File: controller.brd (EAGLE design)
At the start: 100 x 80 mm, 14 parts, among them IC1 7805DT, J1 POWER_JACKSLT, Q1 MOSFET-NCHANNELBSS123LT1G, Q2 MOSFET-PCHANNELSMD

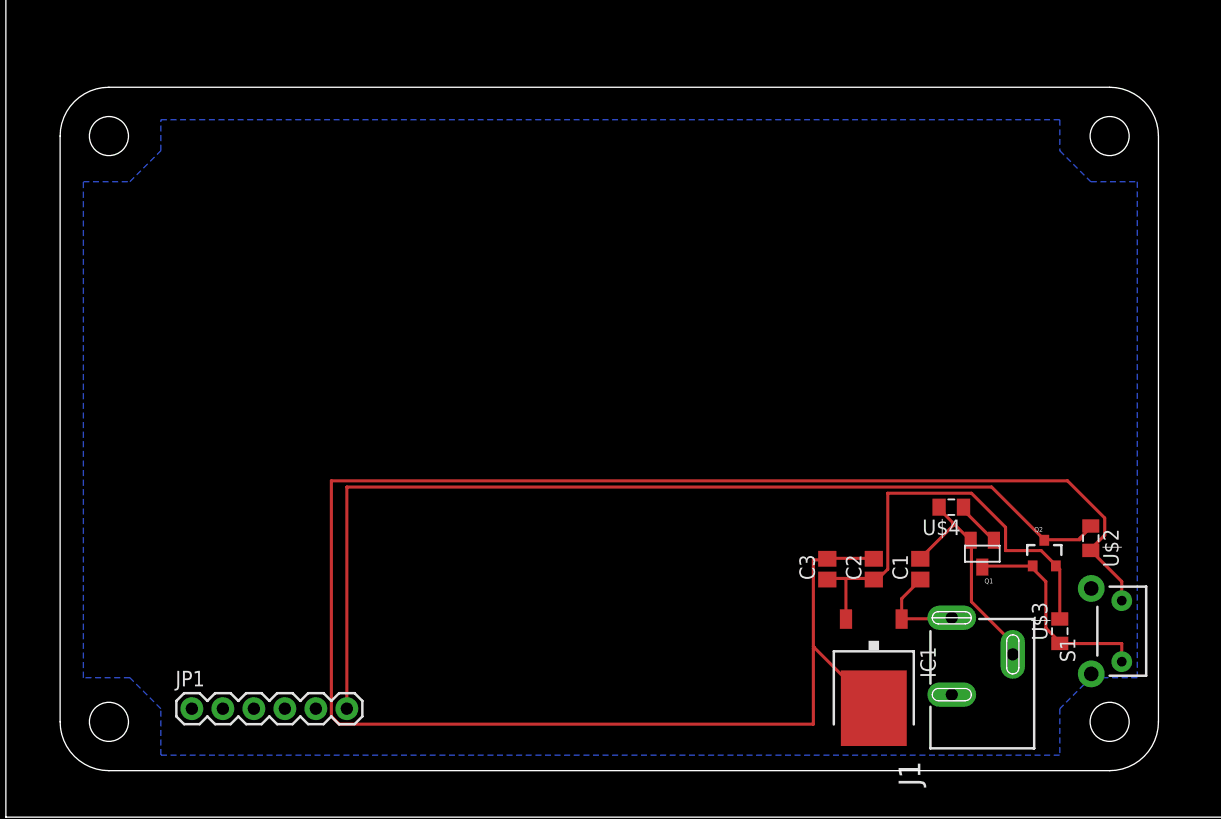
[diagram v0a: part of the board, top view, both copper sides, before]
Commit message: removed parts order from repo
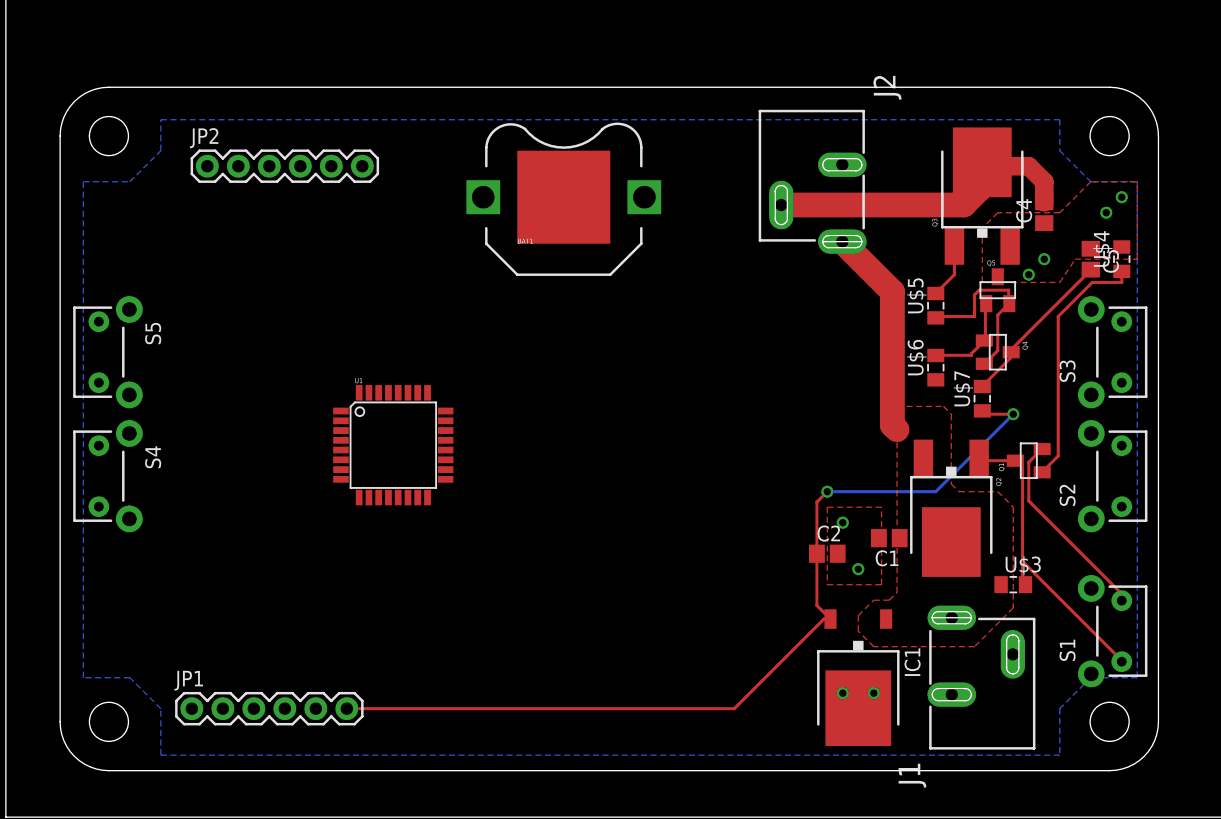
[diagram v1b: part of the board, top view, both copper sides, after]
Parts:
- removed C3: (no value), adafruit:C0805
- removed U$2: (no value), jt_parts:RESISTOR-0805
- added BAT1: (no value), SparkFun-Electromechanical:BATTCON_12MM_PTH
- added C4, C5: (no value), adafruit:C0805
- added J2: POWER_JACKSLT, SparkFun-Connectors:POWER_JACK_SLOT
- added JP2: (no value), SparkFun-Connectors:1X06
- added Q3: MOSFET-NCHANNELFDD8780, SparkFun-DiscreteSemi:DPAK
- added Q4: (no value), SparkFun-DiscreteSemi:SOT23
- added Q5: MMBT4403, SparkFun-DiscreteSemi:SOT23
- added S2, S3, S4, S5: SWITCH-MOMENTARY-2SIDE_EZ, SparkFun-Electromechanical:TACTILE-PTH-SIDEEZ
- added U$5, U$6, U$7: (no value), jt_parts:RESISTOR-0805
- added U1: ATMEGA328P, SparkFun-DigitalIC:TQFP32-08
- Q2: value MOSFET-PCHANNELSMD -> MOSFET-NCHANNELFDD8780; device SparkFun-DiscreteSemi:SOT23-3 -> SparkFun-DiscreteSemi:DPAK
- U$3, U$4: value (none) -> 10k
- moved U$4 24.7 mm to (91.4, 45.7), turned to 90 degrees
- moved Q1 8.52 mm to (83.8, 29.2), turned to 90 degrees
- moved Q2 8.03 mm to (77.5, 24.1), turned to 180 degrees
- moved U$3 5.39 mm to (82.5, 19.1), turned to 0 degrees
- moved C2 4.02 mm to (67.3, 21.6), turned to 0 degrees
- moved C1 3.59 mm to (72.4, 22.9), turned to 180 degrees
- moved IC1 1.27 mm to (69.8, 11.4)
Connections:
- net GATE-MCU renamed PWR-CNTRL
- removed net N$1: C2.1, C3.1, IC1.2, Q2.2, U$3.2
- new net +: BAT1.VCC@1
- new net -: BAT1.GND
- new net 12V-IN: J1.PWR, Q2.4, U$3.1
- new net N$10: Q1.3, Q2.1, S1.1, U$3.2
- new net N$3: Q3.1, U$5.2
- new net N$4: C4.2, J2.GND@2, Q3.4
- new net N$5: Q4.2, Q5.2, U$5.1
- new net NONE: Q4.1, Q5.1, U$6.2
- new net PWM: U$6.1
- net 12V: now also J2.PWR, Q2.3; no longer J1.PWR
- net 5V: now also C2.1, IC1.2, U$7.1; no longer Q2.3, U$2.1
- net GND: now also C4.1, C5.1, Q3.3, Q5.3; no longer C3.2, U$2.2
- net N$2: now also C5.2, Q4.3, U$7.2; no longer Q1.3, Q2.1, S1.1, U$3.1
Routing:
- net GND: track 176.3 -> 19.6 mm, vias 0 -> 8
- net N$1: track 36.9 -> 0.00 mm
- net N$4: track 0.00 -> 26.5 mm
- net N$10: track 0.00 -> 25.9 mm
- net PWR-CNTRL: track 3.76 -> 20.6 mm
- net N$5: track 0.00 -> 14.9 mm
- net 12V: track 8.04 -> 17.3 mm
- net NONE: track 0.00 -> 7.68 mm
- net 5V: track 81.6 -> 74.4 mm, vias 0 -> 2
- net N$2: track 18.1 -> 13.3 mm
- net N$3: track 0.00 -> 4.48 mm
- added copper zone on layer 1, net 12V
- added copper zone on layer 1, net GND

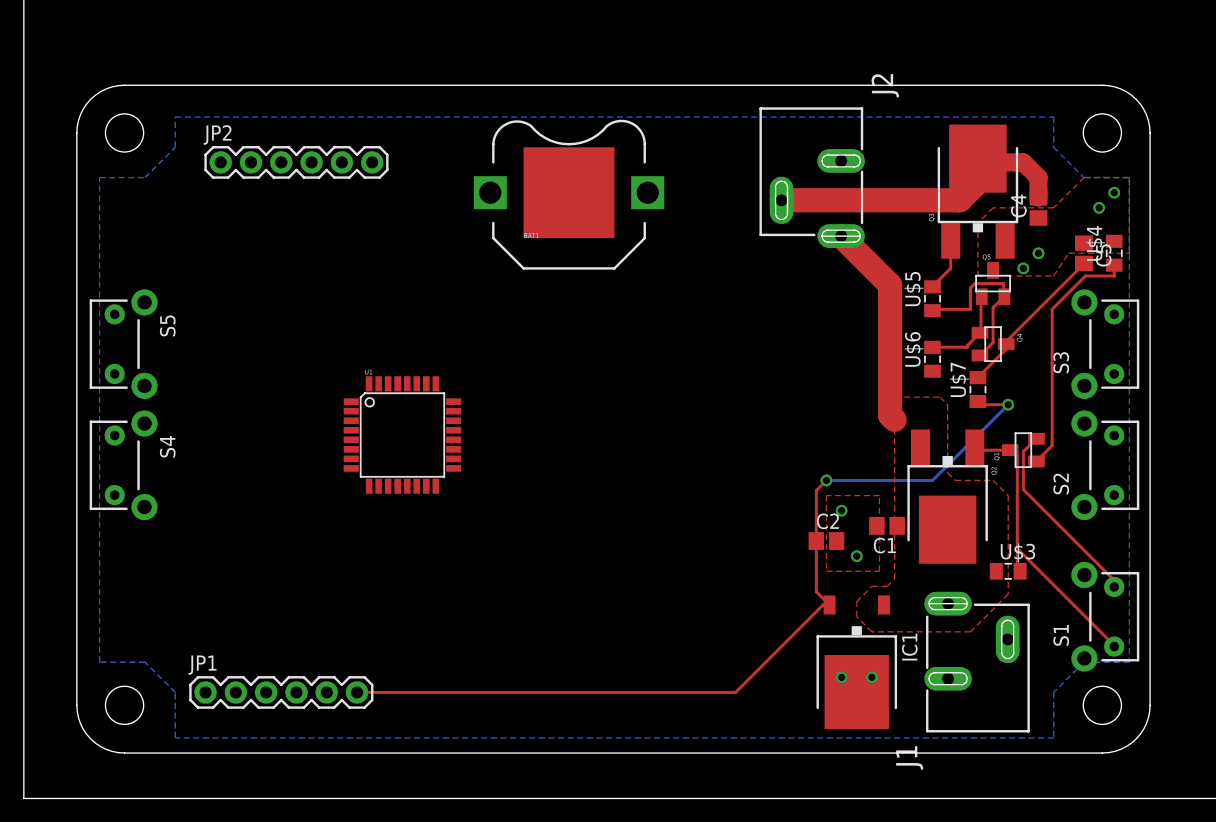
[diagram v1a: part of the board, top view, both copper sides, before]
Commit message: reoriented controller to match with display.
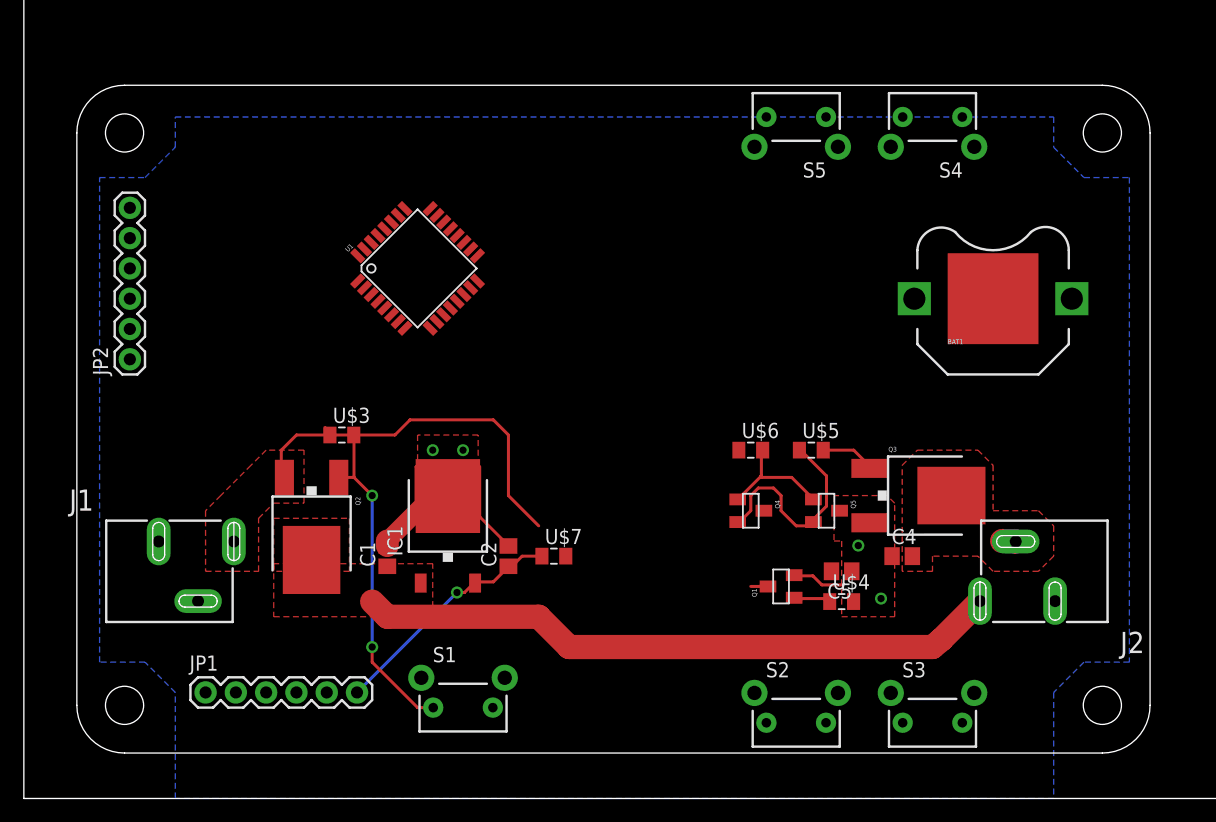
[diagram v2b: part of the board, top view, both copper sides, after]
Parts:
- Q2: value MOSFET-NCHANNELFDD8780 -> MOSFET-PCHANNEL
- moved S4 74.5 mm to (76.2, 57.1), turned to 180 degrees
- moved J1 74.3 mm to (3.81, 24.1), turned to 270 degrees
- moved S5 60.2 mm to (64.8, 57.1), turned to 180 degrees
- moved U$3 57.0 mm to (26.7, 30.5)
- moved S1 55.1 mm to (36.8, 7.62), turned to 0 degrees
- moved Q2 53.4 mm to (24.1, 21.6)
- moved J2 52.3 mm to (94.0, 14.0), turned to 90 degrees
- moved C1 42.0 mm to (30.5, 20.3), turned to 90 degrees
- moved U$7 38.2 mm to (44.5, 20.3), turned to 0 degrees
- moved U$4 37.1 mm to (68.6, 16.5), turned to 0 degrees
- moved BAT1 36.7 mm to (81.3, 41.9)
- moved IC1 36.1 mm to (35.6, 22.9), turned to 0 degrees
- moved S3 35.2 mm to (76.2, 6.35), turned to 0 degrees
- moved S2 34.3 mm to (64.8, 6.35), turned to 0 degrees
- moved C5 33.5 mm to (68.6, 19.1), turned to 180 degrees
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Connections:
- net N$4 renamed 12V-RETURN
- net 12V: now also Q2.4; no longer Q2.3
- net 12V-IN: now also Q2.3; no longer Q2.4
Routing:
- net 5V: track 74.4 -> 20.4 mm, vias 2 -> 1
- net 12V: track 17.3 -> 54.1 mm
- net N$10: track 25.9 -> 55.3 mm, vias 0 -> 2
- net 12V-RETURN: track 26.5 -> 2.55 mm
- net PWR-CNTRL: track 20.6 -> 3.27 mm
- net N$2: track 13.3 -> 0.12 mm
- net GND: track 19.6 -> 31.1 mm, vias 8 -> 4
- net 12V-IN: track 0.00 -> 7.02 mm
- net N$5: track 14.9 -> 18.0 mm
- net NONE: track 7.68 -> 10.3 mm
- added copper zone on layer 1, net 12V-IN
- added copper zone on layer 1, net 12V-RETURN

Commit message: fixed inconsistency between board and schematic.
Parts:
- added C3: (no value), adafruit:E22-10
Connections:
- new net 3.3V: C3.-
- net GND: no longer C5.1
- net N$2: now also C3.+; no longer C5.2
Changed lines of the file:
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@@
 <element name="S2" library="SparkFun-Electromechanical" package="TACTILE-PTH-SIDEEZ" value="SWITCH-MOMENTARY-2SIDE_EZ" x="64.77" y="6.35"/>
 <element name="S3" library="SparkFun-Electromechanical" package="TACTILE-PTH-SIDEEZ" value="SWITCH-MOMENTARY-2SIDE_EZ" x="76.2" y="6.35"/>
+<element name="C3" library="adafruit" package="E22-10" value="" x="53.34" y="27.94" rot="R270"/>
 </elements>
 <signals>
@@
 <contactref element="Q5" pad="3"/>
 <contactref element="U$4" pad="2"/>
-<contactref element="C5" pad="1"/>
 <polygon width="0.254" layer="1" isolate="0.254" thermals="no">
 <vertex x="67.945" y="25.4"/>
@@
 <vertex x="88.9" y="11.43"/>
 <vertex x="86.36" y="8.89"/>
-<vertex x="86.36" y="0"/>
-<vertex x="12.7" y="0"/>
+<vertex x="86.36" y="6.35"/>
+<vertex x="12.7" y="6.35"/>
 <vertex x="12.7" y="8.89"/>
 <vertex x="10.16" y="11.43"/>
@@
 <wire x1="34.907284375" y1="26.017284375" x2="35.56" y2="26.67" width="1.524" layer="1"/>
 <via x="69.977" y="21.209" extent="1-16" drill="0.6096"/>
+<wire x1="69.977" y1="21.209" x2="70.89" y2="23.12" width="0" layer="19" extent="1-1"/>
+<wire x1="68.41" y1="24.13" x2="70.89" y2="23.12" width="0" layer="19" extent="1-1"/>
+<wire x1="72.81" y1="20.32" x2="69.977" y2="21.209" width="0" layer="19" extent="1-1"/>
+<wire x1="68.58" y1="17.907" x2="69.977" y2="21.209" width="0" layer="19" extent="1-1"/>
+<wire x1="69.58" y1="16.51" x2="68.58" y2="17.907" width="0" layer="19" extent="1-1"/>
+<wire x1="71.882" y1="16.764" x2="69.58" y2="16.51" width="0" layer="19" extent="1-1"/>
+<wire x1="40.64" y1="21.17" x2="64.6" y2="18.73" width="0" layer="19" extent="1-1"/>
+<wire x1="36.83" y1="29.21" x2="38.227" y2="27.813" width="0" layer="19" extent="1-1"/>
+<wire x1="34.29" y1="29.21" x2="32.893" y2="27.813" width="0" layer="19" extent="1-1"/>
+<wire x1="39.33" y1="7.62" x2="40.64" y2="21.17" width="0" layer="19" extent="1-1"/>
+<wire x1="14.61" y1="16.55" x2="30.48" y2="21.17" width="0" layer="19" extent="1-1"/>
+<wire x1="17.78" y1="8.89" x2="14.61" y2="16.55" width="0" layer="19" extent="1-1"/>
 </signal>
 <signal name="RCK">
@@
 <signal name="N$2">
 <contactref element="Q4" pad="3"/>
-<contactref element="C5" pad="2"/>
 <contactref element="U$7" pad="2"/>
-<wire x1="61.976" y1="21.59" x2="61.9125" y2="21.5265" width="0" layer="19" extent="1-16"/>
-<wire x1="61.9125" y1="21.5265" x2="60.706" y2="20.32" width="0" layer="19" extent="1-16"/>
-<wire x1="61.976" y1="24.13" x2="61.976" y2="21.59" width="0" layer="19" extent="1-16"/>
-<wire x1="60.706" y1="20.32" x2="45.45" y2="20.32" width="0" layer="19" extent="1-16"/>
 <wire x1="61.976" y1="24.13" x2="62.06" y2="24.13" width="0.254" layer="1"/>
-<wire x1="65.278" y1="21.463" x2="67.691" y2="19.05" width="0" layer="19" extent="1-16"/>
-<wire x1="61.976" y1="21.463" x2="65.278" y2="21.463" width="0" layer="19" extent="1-16"/>
-<wire x1="67.691" y1="19.05" x2="67.73" y2="19.05" width="0.254" layer="1"/>
-<wire x1="61.976" y1="21.463" x2="61.9125" y2="21.5265" width="0" layer="19" extent="1-16"/>
+<contactref element="C3" pad="+"/>
+<wire x1="61.976" y1="24.13" x2="53.34" y2="39.37" width="0" layer="19" extent="1-1"/>
+<wire x1="45.45" y1="20.32" x2="61.976" y2="24.13" width="0" layer="19" extent="1-1"/>
 </signal>
 <signal name="PWM">
@@
 <wire x1="21.59" y1="27.16" x2="21.85" y2="26.9" width="0.254" layer="1"/>
 </signal>
-<signal name="12V-RETURN">
+<signal name="12V-RETURN" class="1">
 <polygon width="0.254" layer="1">
 <vertex x="73.66" y="19.05"/>
@@
 <wire x1="82.042" y1="21.59" x2="83.18" y2="21.55" width="2.032" layer="1"/>
 </signal>
+<signal name="3.3V">
+<contactref element="C3" pad="-"/>
+</signal>
 </signals>
